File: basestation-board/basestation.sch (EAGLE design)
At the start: 22 parts, among them IC1 STM32F0, SW1 ROTARTY_ENCODER, U2 MCP73831, X1 BU-SMA-V, X2 RN4020

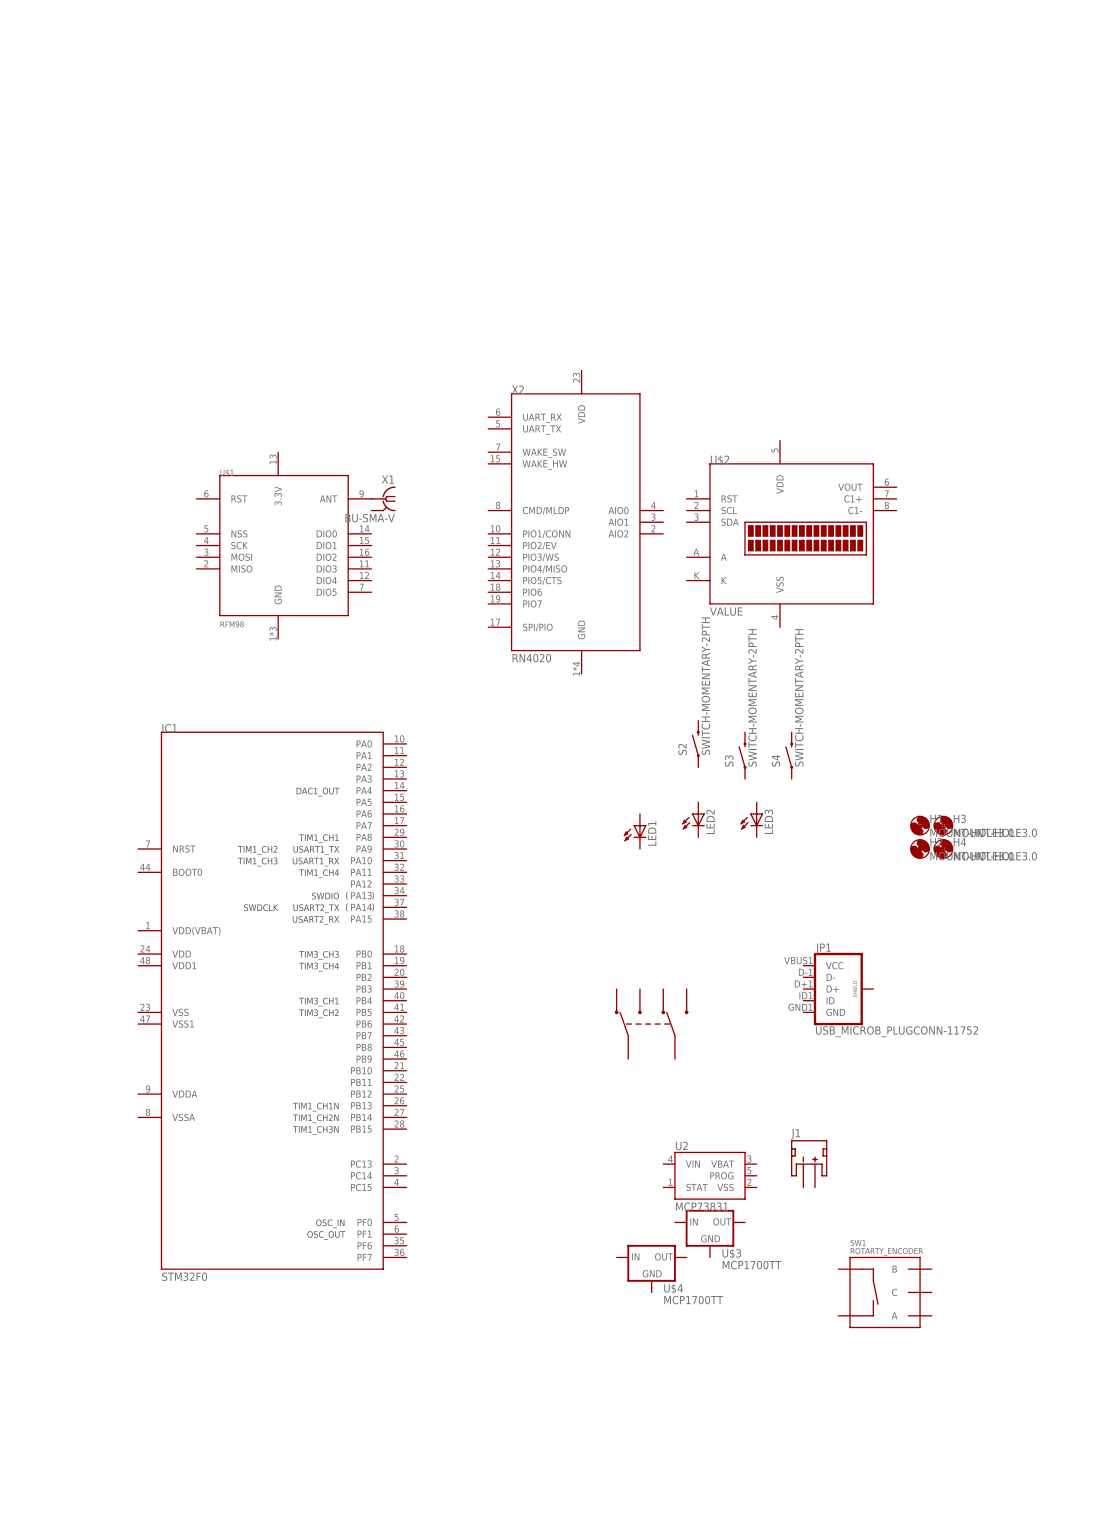
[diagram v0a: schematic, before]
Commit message: added boot0 to tracker, some wiring on basestation
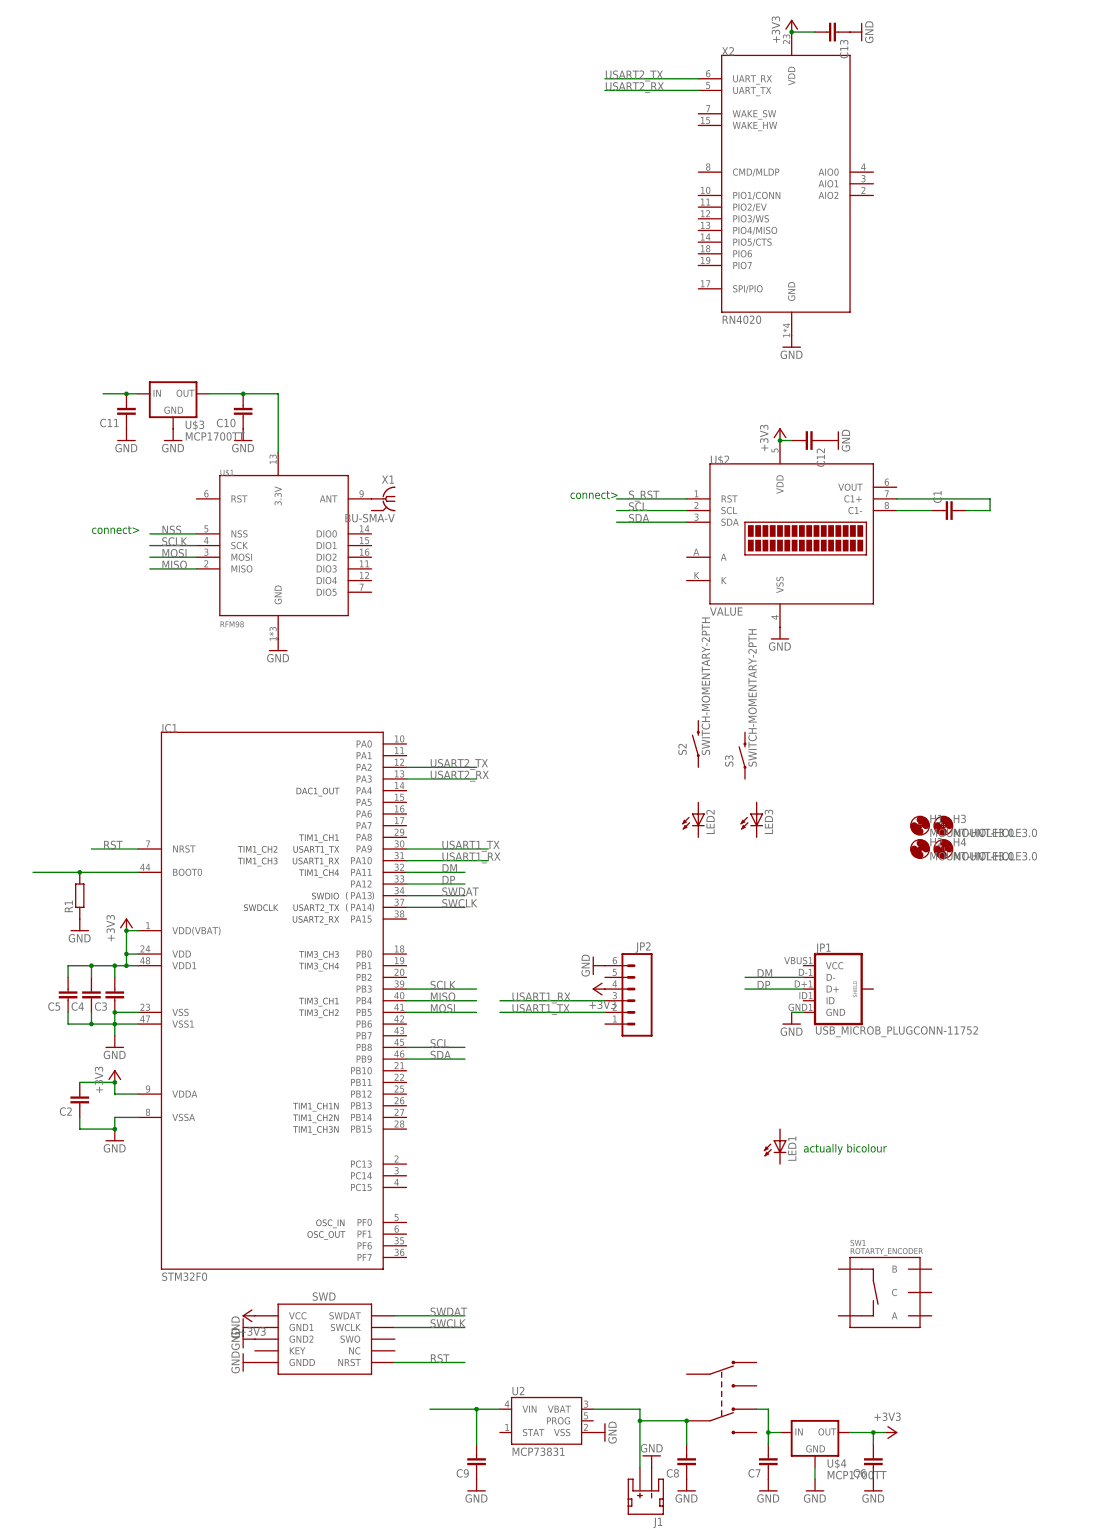
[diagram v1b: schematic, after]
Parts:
- removed S4: SWITCH-MOMENTARY-2PTH, Mine:SWITCH-MOMENTARY-2PTH
- added C1, C10, C11, C12, C13, C2, C3, C4, C5, C6, C7, C8, C9: (no value), resistor:C-EUC0603
- added J2: SWD_PTH_SHROUD, dtb:SWD_PTH_SHROUD
- added JP2: (no value), SparkFun-Connectors:M06SMD
- added R1: (no value), resistor:R-EU_R0603
- LED1: device led:LED3MM -> led:LED5MM
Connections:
- new net +3V3: C12.2, C13.2, C2.2, C3.2, C4.2, C5.2, C6.2, IC1.VDD, IC1.VDD(VBAT), IC1.VDD1, IC1.VDDA, J2.VCC, JP2.4, U$2.VDD, U$4.OUT, X2.VDD
- new net 3.3V: C10.2, U$1.3.3V, U$3.OUT
- new net DM: IC1.PA11, JP1.D-
- new net DP: IC1.PA12, JP1.D+
- new net GND: C10.1, C11.1, C12.1, C13.1, C2.1, C3.1, C4.1, C5.1, C6.1, C7.1, C8.1, C9.1, IC1.VSS, IC1.VSS1, IC1.VSSA, J1.-, J2.GND1, J2.GND2, J2.GNDD, JP1.GND, JP2.6, R1.1, U$1.GND, U$2.VSS, U$3.GND, U$4.GND, U2.VSS, X2.GND
- new net MISO: IC1.PB4, U$1.MISO
- new net MOSI: IC1.PB5, U$1.MOSI
- new net N$2: C8.2, J1.+, U$5.COM1, U2.VBAT
- new net N$3: C7.2, U$4.IN, U$5.NC1
- new net N$4: IC1.BOOT0, R1.2
- new net N$5: C11.2, U$3.IN
- new net N$7: C9.2, U2.VIN
- new net N$8: C1.1, U$2.C1-
- new net N$9: C1.2, U$2.C1+
- new net NSS: U$1.NSS
- new net RST: IC1.NRST, J2.NRST
- new net SCL: IC1.PB8, U$2.SCL
- new net SCLK: IC1.PB3, U$1.SCK
- new net SDA: IC1.PB9, U$2.SDA
- new net SWCLK: IC1.PA14, J2.SWCLK
- new net SWDAT: IC1.PA13, J2.SWDAT
- new net S_RST: U$2.RST
- new net USART1_RX: IC1.PA10, JP2.3
- new net USART1_TX: IC1.PA9, JP2.2
- new net USART2_RX: IC1.PA3, X2.UART_TX
- new net USART2_TX: IC1.PA2, X2.UART_RX
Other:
- note added: "actually bicolour"
- note added: "connect>"
- moved on the sheet: J1, LED1, U$3, U$4, U2, X2

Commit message: initial route
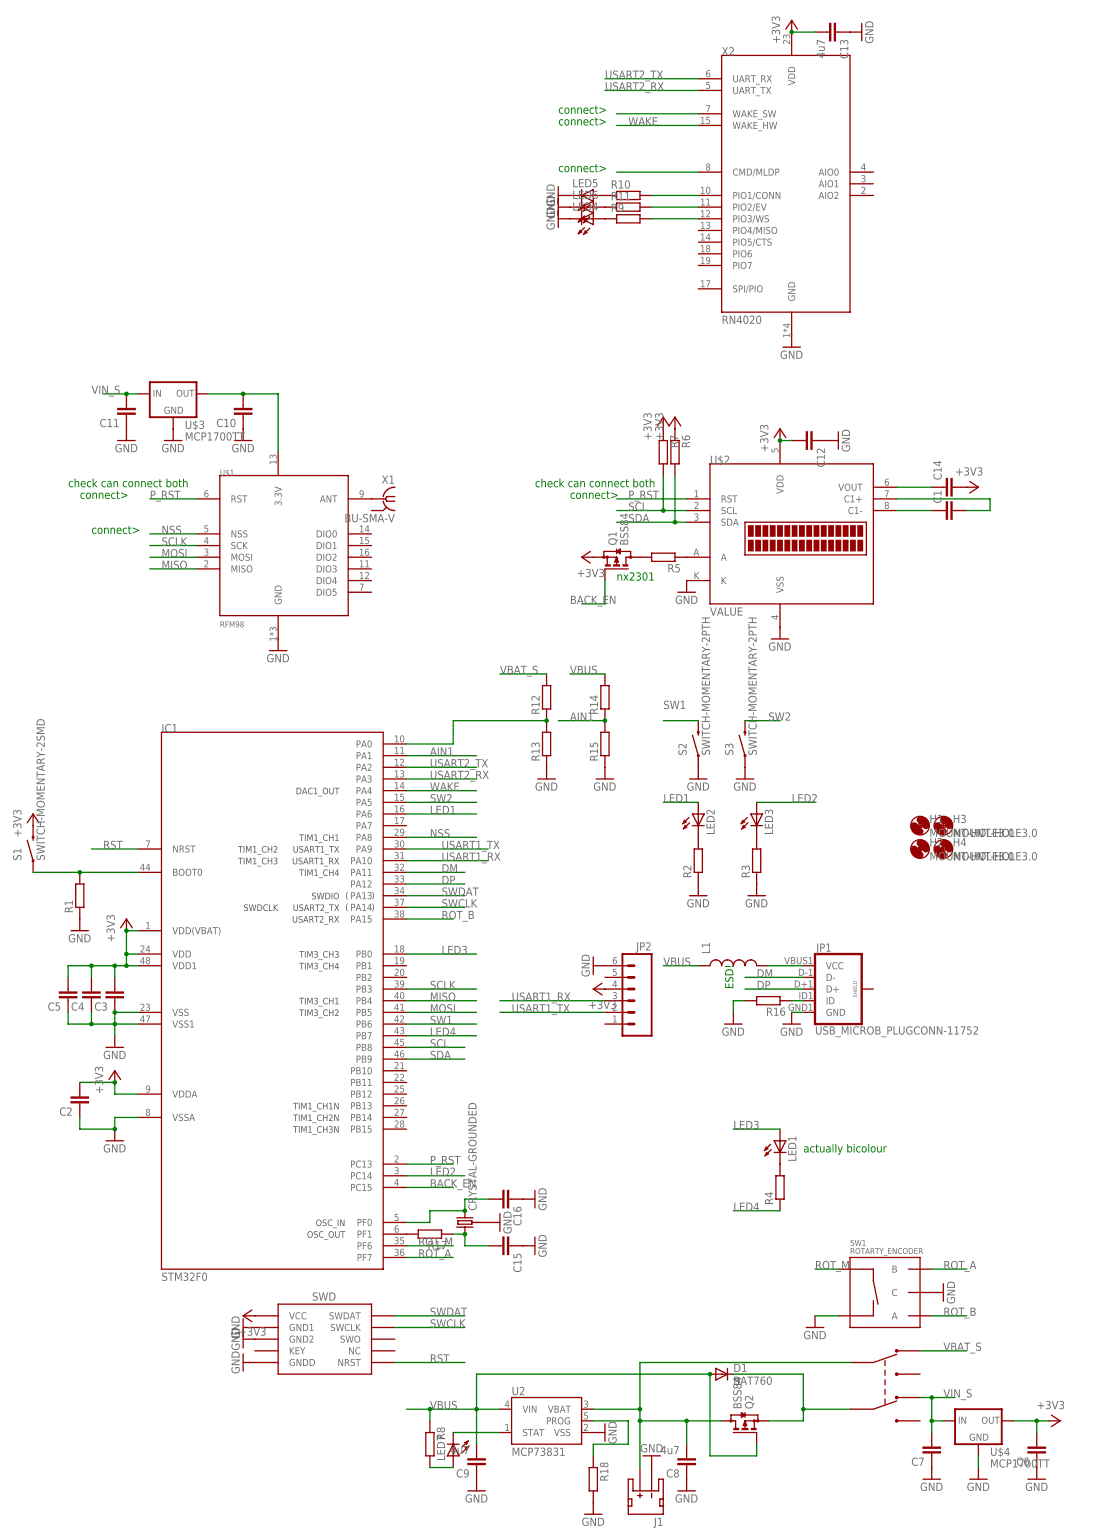
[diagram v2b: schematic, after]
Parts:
- added C14, C15, C16: (no value), resistor:C-EUC0603
- added D1: BAT760, dtb:DIODE-SOD323-R
- added L1: (no value), SparkFun-Passives:INDUCTOR0603
- added LED4, LED5, LED6, LED7: (no value), led:LEDCHIP-LED0805
- added Q1, Q2: BSS84, transistor-small-signal:BSS84
- added R10, R11, R12, R13, R14, R15, R16, R17, R18, R2, R3, R4, R5, R6, R7, R8, R9: (no value), resistor:R-EU_R0603
- added S1: SWITCH-MOMENTARY-2SMD, Mine:SWITCH-MOMENTARY-2SMD
- added U$6: CRYSTAL-GROUNDED, SparkFun-FreqCtrl:CRYSTAL-GROUNDED
- C13, C8, C9: value (none) -> 4u7
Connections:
- removed net S_RST: U$2.RST
- new net AIN1: IC1.PA1, R14.1, R15.2
- new net BACK_EN: IC1.PC15, Q1.G
- new net LED1: IC1.PA6, LED2.A
- new net LED2: IC1.PC14, LED3.A
- new net LED3: IC1.PB0, LED1.A
- new net LED4: IC1.PB7, R4.1
- new net N$10: LED3.C, R3.2
- new net N$11: LED1.C, R4.2
- new net N$12: C14.1, U$2.VOUT
- new net N$13: R11.2, X2.PIO2/EV
- new net N$14: R9.2, X2.PIO3/WS
- new net N$15: LED5.A, R10.1
- new net N$16: LED6.A, R11.1
- new net N$17: LED4.A, R9.1
- new net N$18: X2.WAKE_SW
- new net N$19: X2.CMD/MLDP
- new net N$23: R5.1, U$2.A
- new net N$27: IC1.PA0, R12.1, R13.2
- new net N$28: JP1.ID, R16.1
- new net N$29: LED7.C, U2.STAT
- new net N$30: IC1.PF1, R17.2
- new net N$31: C16.2, IC1.PF0, U$6.2
- new net N$32: C15.2, R17.1, U$6.1
- new net N$33: C8.2, J1.+, Q2.D, U$5.COM0, U2.VBAT
- new net N$34: LED7.A, R8.2
- new net N$35: JP1.VCC, L1.2
- new net N$6: LED2.C, R2.2
- new net P_RST: IC1.PC13, U$1.RST, U$2.RST
- new net ROT_A: IC1.PF7, SW1.B
- new net ROT_B: IC1.PA15, SW1.A
- new net ROT_M: IC1.PF6, SW1.SW+
- new net SW1: IC1.PB6, S2.2
- new net SW2: IC1.PA5, S3.2
- new net VBAT_S: R12.2, U$5.NC0
- new net VBUS: C9.2, D1.A, L1.1, Q2.G, R14.2, R8.1, U2.VIN
- new net VIN_S: C11.2, C7.2, U$3.IN, U$4.IN, U$5.NC1
- new net WAKE: IC1.PA4, X2.WAKE_HW
- net +3V3: now also C14.2, Q1.S, R6.1, R7.1, S1.2
- net GND: now also C15.1, C16.1, LED4.C, LED5.C, LED6.C, R13.1, R15.1, R16.2, R18.2, R2.1, R3.1, S2.1, S3.1, SW1.C, SW1.SW-, U$2.K, U$6.3
- net N$2: now also D1.C, Q2.S; no longer C8.2, J1.+, U2.VBAT
- net N$3: now also Q1.D, R5.2; no longer C7.2, U$4.IN, U$5.NC1
- net N$4: now also S1.1
- net N$5: now also R10.2, X2.PIO1/CONN; no longer C11.2, U$3.IN
- net N$7: now also R18.1, U2.PROG; no longer C9.2, U2.VIN
- net NSS: now also IC1.PA8
- net SCL: now also R7.2
- net SDA: now also R6.2
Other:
- note added: "ESD!"
- note added: "check can connect both"
- note added: "nx2301"
- moved on the sheet: C6, C7, S3, U$4

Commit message: adding interrupt line to raido
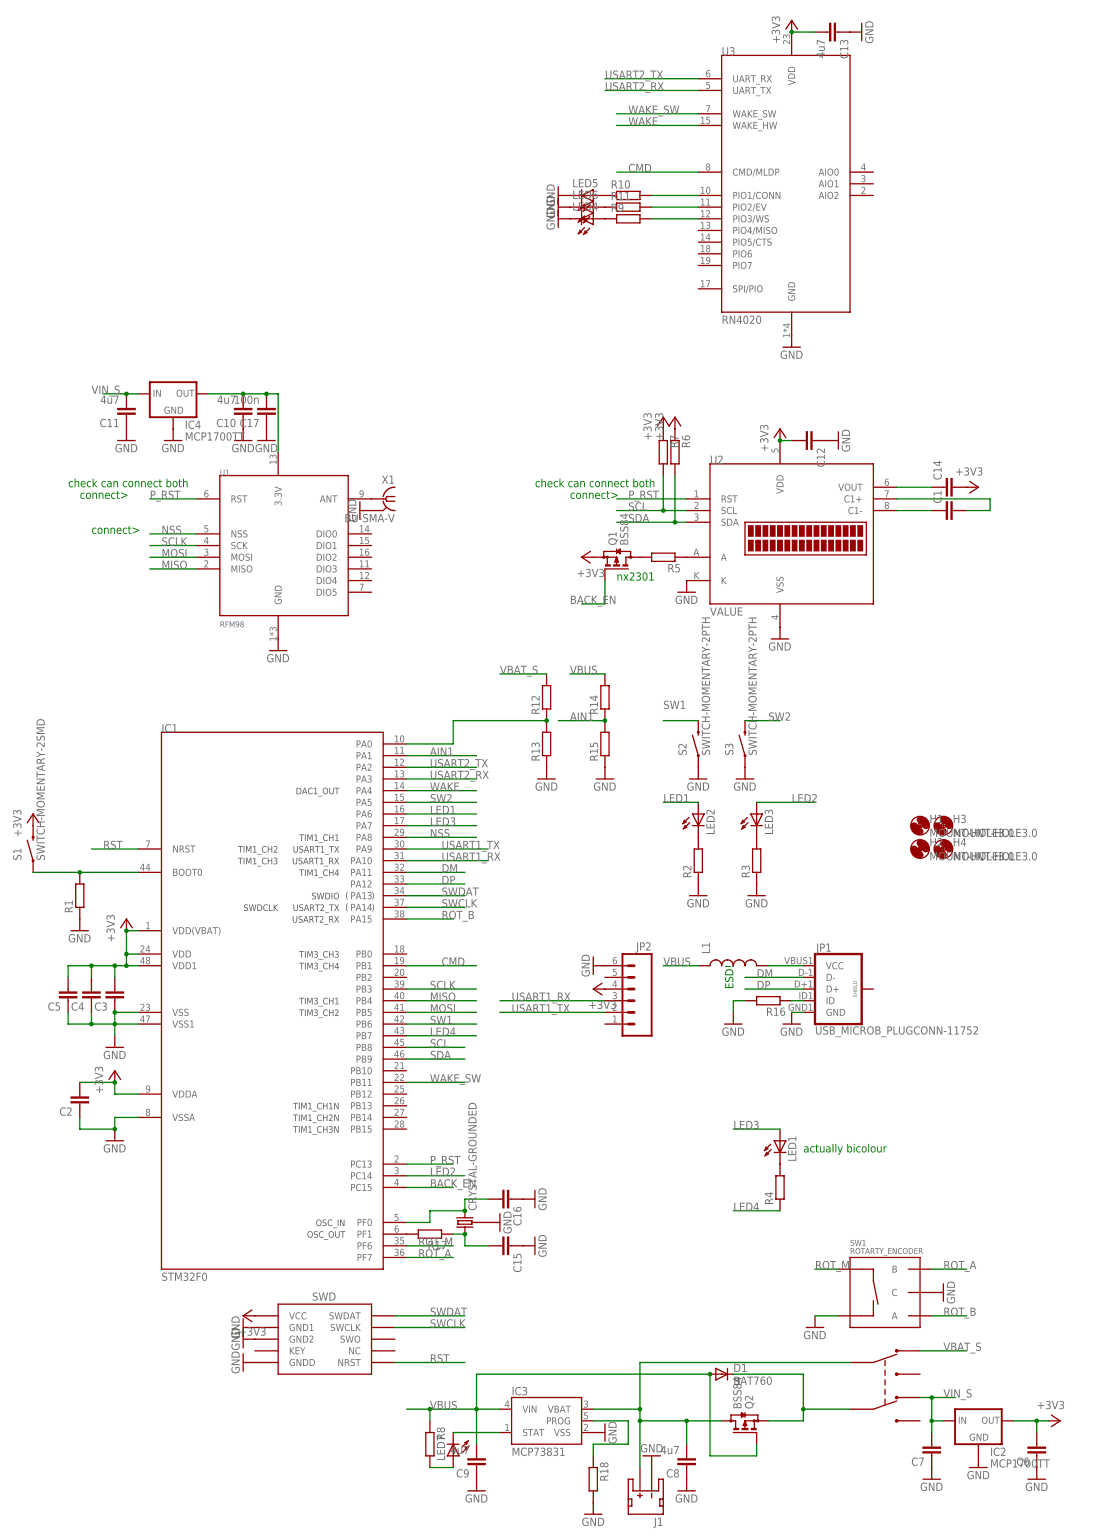
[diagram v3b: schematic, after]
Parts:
- removed U$2: NHD-C0216CIZ-FSW, dtb:NHD-C0216CIZ-FSW
- removed U$6: CRYSTAL-GROUNDED, SparkFun-FreqCtrl:CRYSTAL-GROUNDED
- added C17: 100n, resistor:C-EUC0603
- added IC3: MCP73831, SparkFun-PowerIC:MCP73831
- added U3: RN4020, Mine:RN4020
- C10, C11: value (none) -> 4u7
- U2: value MCP73831 -> NHD-C0216CIZ-FSW; device SparkFun-PowerIC:MCP73831 -> dtb:NHD-C0216CIZ-FSW
- X2: value RN4020 -> CRYSTAL-GROUNDED; device Mine:RN4020 -> SparkFun-FreqCtrl:CRYSTAL-GROUNDED
- renumbered U$1 to U1, U$3 to IC4, U$4 to IC2
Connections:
- removed net N$18: X2.WAKE_SW
- removed net N$19: X2.CMD/MLDP
- new net CMD: IC1.PB1, U3.CMD/MLDP
- new net WAKE_SW: IC1.PB11, U3.WAKE_SW
- net +3V3: now also U2.VDD, U3.VDD; no longer U$2.VDD, X2.VDD
- net 3.3V: now also C17.2
- net GND: now also C17.1, IC3.VSS, U2.K, U3.GND, X1.2, X2.3; no longer U$2.K, U$2.VSS, U$6.3, X2.GND
- net LED3: now also IC1.PA7; no longer IC1.PB0
- net N$12: now also U2.VOUT; no longer U$2.VOUT
- net N$13: now also U3.PIO2/EV; no longer X2.PIO2/EV
- net N$14: now also U3.PIO3/WS; no longer X2.PIO3/WS
- net N$23: now also U2.A; no longer U$2.A
- net N$29: now also IC3.STAT; no longer U2.STAT
- net N$31: now also X2.2; no longer U$6.2
- net N$32: now also X2.1; no longer U$6.1
- net N$33: now also IC3.VBAT; no longer U2.VBAT
- net N$5: now also U3.PIO1/CONN; no longer X2.PIO1/CONN
- net N$7: now also IC3.PROG; no longer U2.PROG
- net N$8: now also U2.C1-; no longer U$2.C1-
- net N$9: now also U2.C1+; no longer U$2.C1+
- net P_RST: now also U2.RST; no longer U$2.RST
- net SCL: now also U2.SCL; no longer U$2.SCL
- net SDA: now also U2.SDA; no longer U$2.SDA
- net USART2_RX: now also U3.UART_TX; no longer X2.UART_TX
- net USART2_TX: now also U3.UART_RX; no longer X2.UART_RX
- net VBUS: now also IC3.VIN; no longer U2.VIN
- net WAKE: now also U3.WAKE_HW; no longer X2.WAKE_HW
